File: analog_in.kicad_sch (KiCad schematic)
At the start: 0 parts

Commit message: Routed analog input and generator, added ethernet
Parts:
- added C2: 0.1, symbol Device:C
- added D5: TVS, Package_TO_SOT_SMD:SOT-23, symbol Diode:SM712_SOT23
- added R13, R14: 100, symbol Device:R
- added U2: INA600, Package_TO_SOT_SMD:SOT-23-6, symbol Amplifier_Current:INA181
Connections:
- new net: D5.1 (A1), R13.2, U2.3 (+)
- new net: D5.2 (A2), R14.2, U2.4 (-)
- new net +1V8: U2.5 (REF)
- new net +5V: C2.2, U2.6 (V+)
- new net AIN+: R13.1
- new net AIN-: R14.1
- new net AOUT: U2.1
- new net GND: C2.1, D5.3 (common), U2.2 (GND)

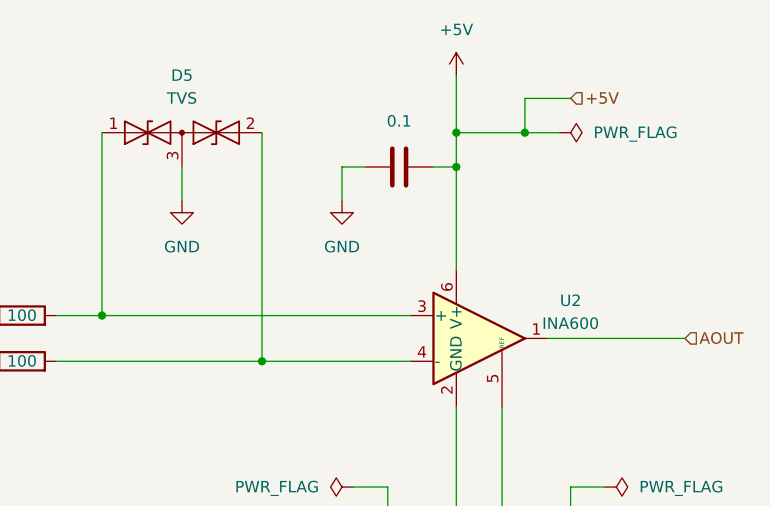
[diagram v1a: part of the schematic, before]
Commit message: Rearranged sheets and corrected some namings
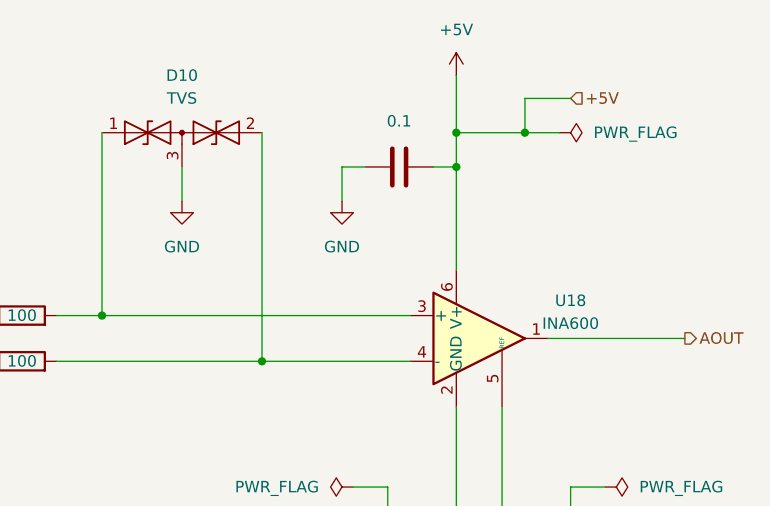
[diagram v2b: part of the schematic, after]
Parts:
- renumbered C2 to C40, D5 to D10, R13 to R43, R14 to R44, U2 to U18

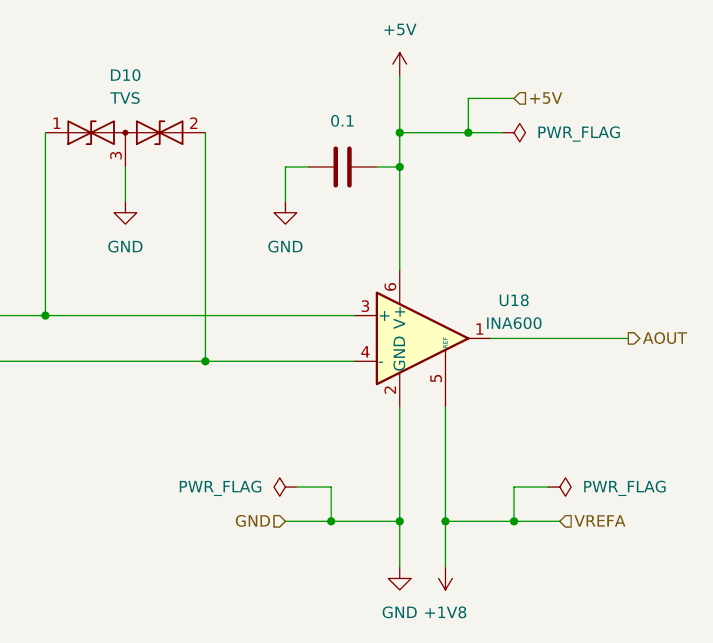
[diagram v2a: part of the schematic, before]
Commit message: Finished power setup and cleared some mistakes
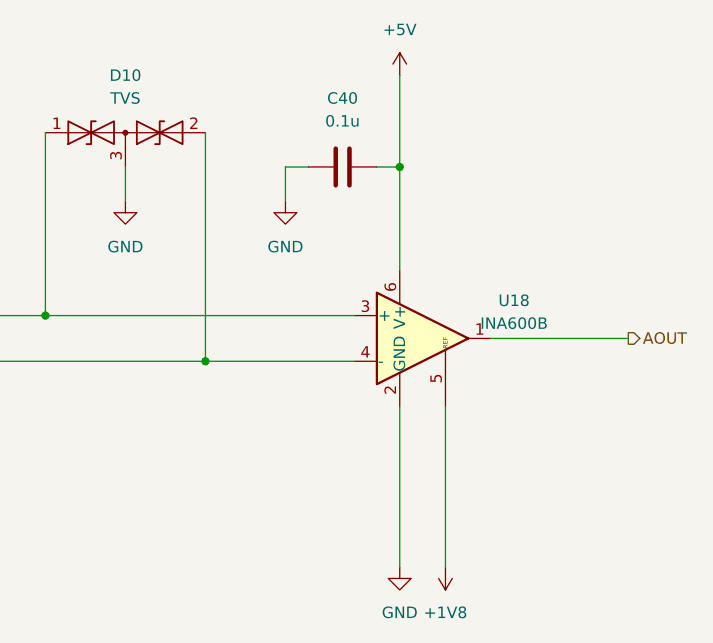
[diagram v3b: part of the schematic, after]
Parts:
- C40: value 0.1 -> 0.1u
- U18: value INA600 -> INA600B
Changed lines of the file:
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@@
 (kicad_sch (version 20230121) (generator eeschema)
   (paper "A4")
-  (junction (at 165.1 115.57) (diameter 0) (color 0 0 0 0)
-  )
-  (junction (at 165.1 72.39) (diameter 0) (color 0 0 0 0)
-  )
-  (junction (at 170.18 115.57) (diameter 0) (color 0 0 0 0)
-  )
-  (junction (at 172.72 72.39) (diameter 0) (color 0 0 0 0)
-  )
-  (junction (at 177.8 115.57) (diameter 0) (color 0 0 0 0)
-  )
-  (junction (at 157.48 115.57) (diameter 0) (color 0 0 0 0)
-  )
   (junction (at 165.1 76.2) (diameter 0) (color 0 0 0 0)
   )
@@
   (junction (at 143.51 97.79) (diameter 0) (color 0 0 0 0)
   )
-  (wire (pts (xy 170.18 115.57) (xy 177.8 115.57))
-    (stroke (width 0) (type default))
-  )
-  (wire (pts (xy 177.8 115.57) (xy 182.88 115.57))
-    (stroke (width 0) (type default))
-  )
-  (wire (pts (xy 181.61 111.76) (xy 177.8 111.76))
-    (stroke (width 0) (type default))
-  )
-  (wire (pts (xy 172.72 72.39) (xy 176.53 72.39))
-    (stroke (width 0) (type default))
-  )
   (wire (pts (xy 102.87 97.79) (xy 113.03 97.79))
     (stroke (width 0) (type default))
@@
     (stroke (width 0) (type default))
   )
-  (wire (pts (xy 157.48 111.76) (xy 157.48 115.57))
-    (stroke (width 0) (type default))
-  )
   (wire (pts (xy 143.51 97.79) (xy 160.02 97.79))
     (stroke (width 0) (type default))
   )
-  (wire (pts (xy 165.1 66.04) (xy 165.1 72.39))
-    (stroke (width 0) (type default))
-  )
-  (wire (pts (xy 152.4 115.57) (xy 157.48 115.57))
+  (wire (pts (xy 165.1 66.04) (xy 165.1 76.2))
     (stroke (width 0) (type default))
   )
@@
     (stroke (width 0) (type default))
   )
-  (wire (pts (xy 170.18 102.87) (xy 170.18 115.57))
+  (wire (pts (xy 170.18 102.87) (xy 170.18 120.65))
     (stroke (width 0) (type default))
   )
@@
     (stroke (width 0) (type default))
   )
-  (wire (pts (xy 165.1 102.87) (xy 165.1 115.57))
+  (wire (pts (xy 165.1 102.87) (xy 165.1 120.65))
     (stroke (width 0) (type default))
   )
@@
     (stroke (width 0) (type default))
   )
-  (wire (pts (xy 170.18 115.57) (xy 170.18 120.65))
-    (stroke (width 0) (type default))
-  )
-  (wire (pts (xy 165.1 72.39) (xy 165.1 76.2))
-    (stroke (width 0) (type default))
-  )
   (wire (pts (xy 102.87 92.71) (xy 113.03 92.71))
     (stroke (width 0) (type default))
   )
-  (wire (pts (xy 153.67 111.76) (xy 157.48 111.76))
-    (stroke (width 0) (type default))
-  )
-  (wire (pts (xy 177.8 111.76) (xy 177.8 115.57))
-    (stroke (width 0) (type default))
-  )
-  (wire (pts (xy 172.72 68.58) (xy 172.72 72.39))
-    (stroke (width 0) (type default))
-  )
   (wire (pts (xy 152.4 76.2) (xy 152.4 80.01))
     (stroke (width 0) (type default))
   )
-  (wire (pts (xy 177.8 68.58) (xy 172.72 68.58))
-    (stroke (width 0) (type default))
-  )
   (wire (pts (xy 125.73 72.39) (xy 125.73 92.71))
     (stroke (width 0) (type default))
   )
-  (wire (pts (xy 157.48 115.57) (xy 165.1 115.57))
-    (stroke (width 0) (type default))
-  )
   (wire (pts (xy 120.65 97.79) (xy 143.51 97.79))
     (stroke (width 0) (type default))
   )
-  (wire (pts (xy 165.1 115.57) (xy 165.1 120.65))
-    (stroke (width 0) (type default))
-  )
   (wire (pts (xy 143.51 72.39) (xy 143.51 97.79))
     (stroke (width 0) (type default))
   )
   (wire (pts (xy 134.62 76.2) (xy 134.62 80.01))
-    (stroke (width 0) (type default))
-  )
-  (wire (pts (xy 165.1 72.39) (xy 172.72 72.39))
     (stroke (width 0) (type default))
   )
@@
     (effects (font (size 1.27 1.27)) (justify left))
   )
-  (hierarchical_label "+5V" (shape input) (at 177.8 68.58 0) (fields_autoplaced)
-    (effects (font (size 1.27 1.27)) (justify left))
-  )
-  (hierarchical_label "GND" (shape input) (at 152.4 115.57 180) (fields_autoplaced)
-    (effects (font (size 1.27 1.27)) (justify right))
-  )
   (hierarchical_label "AIN+" (shape input) (at 102.87 92.71 180) (fields_autoplaced)
     (effects (font (size 1.27 1.27)) (justify right))
-  )
-  (hierarchical_label "VREFA" (shape input) (at 182.88 115.57 0) (fields_autoplaced)
-    (effects (font (size 1.27 1.27)) (justify left))
   )
   (hierarchical_label "AIN-" (shape input) (at 102.87 97.79 180) (fields_autoplaced)
@@
     (in_bom yes) (on_board yes) (dnp no) (fields_autoplaced)
     (property "Reference" "C40" (at 158.75 68.58 90)
-      (effects (font (size 1.27 1.27)) hide)
-    )
-    (property "Value" "0.1" (at 158.75 71.12 90)
+      (effects (font (size 1.27 1.27)))
+    )
+    (property "Value" "0.1u" (at 158.75 71.12 90)
       (effects (font (size 1.27 1.27)))
     )
@@
     )
   )
-  (symbol (lib_id "power:PWR_FLAG") (at 181.61 111.76 270) (unit 1)
-    (in_bom yes) (on_board yes) (dnp no) (fields_autoplaced)
-    (property "Reference" "#FLG042" (at 183.515 111.76 0)
-      (effects (font (size 1.27 1.27)) hide)
-    )
-    (property "Value" "PWR_FLAG" (at 185.42 111.76 90)
-      (effects (font (size 1.27 1.27)) (justify left))
-    )
-    (property "Footprint" "" (at 181.61 111.76 0)
-      (effects (font (size 1.27 1.27)) hide)
-    )
-    (property "Datasheet" "~" (at 181.61 111.76 0)
-      (effects (font (size 1.27 1.27)) hide)
-    )
-    (pin "1")
-    (instances
-      (project "cad-enc-dec"
-        (path "/894df1c3-1a5d-48b0-9966-84d5c2c2c705/3147f239-9a8b-459b-8889-8b3ae22f6154"
-          (reference "#FLG042") (unit 1)
-        )
-        (path "/894df1c3-1a5d-48b0-9966-84d5c2c2c705/48b865f7-3ad4-4ab2-8a39-622512f3cca3"
-          (reference "#FLG05") (unit 1)
-        )
-        (path "/894df1c3-1a5d-48b0-9966-84d5c2c2c705/6aec754e-1a09-4013-9dcc-eaf34b4a6299"
-          (reference "#FLG028") (unit 1)
-        )
-        (path "/894df1c3-1a5d-48b0-9966-84d5c2c2c705/03acb586-98c9-4180-936a-eaf01854a57a"
-          (reference "#FLG035") (unit 1)
-        )
-        (path "/894df1c3-1a5d-48b0-9966-84d5c2c2c705/0562ea40-d947-4895-9f9c-71efdb5c7549"
-          (reference "#FLG021") (unit 1)
-        )
-        (path "/894df1c3-1a5d-48b0-9966-84d5c2c2c705/04ed763c-fa4a-4a00-b73b-43854aeae6ba"
-          (reference "#FLG018") (unit 1)
-        )
-      )
-    )
-  )
-  (symbol (lib_id "power:PWR_FLAG") (at 153.67 111.76 90) (unit 1)
-    (in_bom yes) (on_board yes) (dnp no) (fields_autoplaced)
-    (property "Reference" "#FLG041" (at 151.765 111.76 0)
-      (effects (font (size 1.27 1.27)) hide)
-    )
-    (property "Value" "PWR_FLAG" (at 149.86 111.76 90)
-      (effects (font (size 1.27 1.27)) (justify left))
-    )
-    (property "Footprint" "" (at 153.67 111.76 0)
-      (effects (font (size 1.27 1.27)) hide)
-    )
-    (property "Datasheet" "~" (at 153.67 111.76 0)
-      (effects (font (size 1.27 1.27)) hide)
-    )
-    (pin "1")
-    (instances
-      (project "cad-enc-dec"
-        (path "/894df1c3-1a5d-48b0-9966-84d5c2c2c705/3147f239-9a8b-459b-8889-8b3ae22f6154"
-          (reference "#FLG041") (unit 1)
-        )
-        (path "/894df1c3-1a5d-48b0-9966-84d5c2c2c705/48b865f7-3ad4-4ab2-8a39-622512f3cca3"
-          (reference "#FLG04") (unit 1)
-        )
-        (path "/894df1c3-1a5d-48b0-9966-84d5c2c2c705/6aec754e-1a09-4013-9dcc-eaf34b4a6299"
-          (reference "#FLG025") (unit 1)
-        )
-        (path "/894df1c3-1a5d-48b0-9966-84d5c2c2c705/03acb586-98c9-4180-936a-eaf01854a57a"
-          (reference "#FLG034") (unit 1)
-        )
-        (path "/894df1c3-1a5d-48b0-9966-84d5c2c2c705/0562ea40-d947-4895-9f9c-71efdb5c7549"
-          (reference "#FLG020") (unit 1)
-        )
-        (path "/894df1c3-1a5d-48b0-9966-84d5c2c2c705/04ed763c-fa4a-4a00-b73b-43854aeae6ba"
-          (reference "#FLG017") (unit 1)
-        )
-      )
-    )
-  )
   (symbol (lib_id "Amplifier_Current:INA181") (at 167.64 95.25 0) (unit 1)
     (in_bom yes) (on_board yes) (dnp no) (fields_autoplaced)
@@
       (effects (font (size 1.27 1.27)))
     )
-    (property "Value" "INA600" (at 177.8 93.5991 0)
+    (property "Value" "INA600B" (at 177.8 93.5991 0)
       (effects (font (size 1.27 1.27)))
     )
@@
         )
       )
-    )
-  )
-  (symbol (lib_id "power:PWR_FLAG") (at 176.53 72.39 270) (unit 1)
-    (in_bom yes) (on_board yes) (dnp no) (fields_autoplaced)
-    (property "Reference" "#FLG040" (at 178.435 72.39 0)
-      (effects (font (size 1.27 1.27)) hide)
-    )
-    (property "Value" "PWR_FLAG" (at 180.34 72.39 90)
-      (effects (font (size 1.27 1.27)) (justify left))
-    )
-    (property "Footprint" "" (at 176.53 72.39 0)
-      (effects (font (size 1.27 1.27)) hide)
-    )
-    (property "Datasheet" "~" (at 176.53 72.39 0)
-      (effects (font (size 1.27 1.27)) hide)
-    )
-    (pin "1")
-    (instances
-      (project "cad-enc-dec"
-        (path "/894df1c3-1a5d-48b0-9966-84d5c2c2c705/3147f239-9a8b-459b-8889-8b3ae22f6154"
-          (reference "#FLG040") (unit 1)
-        )
-        (path "/894df1c3-1a5d-48b0-9966-84d5c2c2c705/48b865f7-3ad4-4ab2-8a39-622512f3cca3"
-          (reference "#FLG03") (unit 1)
-        )
-        (path "/894df1c3-1a5d-48b0-9966-84d5c2c2c705/6aec754e-1a09-4013-9dcc-eaf34b4a6299"
-          (reference "#FLG024") (unit 1)
-        )
-        (path "/894df1c3-1a5d-48b0-9966-84d5c2c2c705/03acb586-98c9-4180-936a-eaf01854a57a"
-          (reference "#FLG033") (unit 1)
-        )
-        (path "/894df1c3-1a5d-48b0-9966-84d5c2c2c705/0562ea40-d947-4895-9f9c-71efdb5c7549"
-          (reference "#FLG019") (unit 1)
-        )
-        (path "/894df1c3-1a5d-48b0-9966-84d5c2c2c705/04ed763c-fa4a-4a00-b73b-43854aeae6ba"
-          (reference "#FLG016") (unit 1)
-        )
-      )

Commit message: Polished IO schematics
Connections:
- net +1V8 renamed VREFAIN
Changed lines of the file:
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@@
-    (stroke (width 0) (type default))
-  )
-  (wire (pts (xy 170.18 102.87) (xy 170.18 120.65))
     (stroke (width 0) (type default))
   )
@@
     (stroke (width 0) (type default))
   )
+  (wire (pts (xy 170.18 102.87) (xy 170.18 105.41))
+    (stroke (width 0) (type default))
+  )
   (wire (pts (xy 102.87 92.71) (xy 113.03 92.71))
+    (stroke (width 0) (type default))
+  )
+  (wire (pts (xy 139.7 105.41) (xy 170.18 105.41))
     (stroke (width 0) (type default))
   )
@@
   (wire (pts (xy 134.62 76.2) (xy 134.62 80.01))
     (stroke (width 0) (type default))
+  )
+  (hierarchical_label "VREFAIN" (shape input) (at 139.7 105.41 180) (fields_autoplaced)
+    (effects (font (size 1.27 1.27)) (justify right))
   )
   (hierarchical_label "AOUT" (shape output) (at 190.5 95.25 0) (fields_autoplaced)
@@
         )
       )
-    )
-  )
-  (symbol (lib_id "power:+1V8") (at 170.18 120.65 180) (unit 1)
-    (in_bom yes) (on_board yes) (dnp no) (fields_autoplaced)
-    (property "Reference" "#PWR073" (at 170.18 116.84 0)
-      (effects (font (size 1.27 1.27)) hide)
-    )
-    (property "Value" "+1V8" (at 170.18 125.73 0)
-      (effects (font (size 1.27 1.27)))
-    )
-    (property "Footprint" "" (at 170.18 120.65 0)
-      (effects (font (size 1.27 1.27)) hide)
-    )
-    (property "Datasheet" "" (at 170.18 120.65 0)
-      (effects (font (size 1.27 1.27)) hide)
-    )
-    (pin "1")
-    (instances
-      (project "cad-enc-dec"
-        (path "/894df1c3-1a5d-48b0-9966-84d5c2c2c705/3147f239-9a8b-459b-8889-8b3ae22f6154"
-          (reference "#PWR073") (unit 1)
-        )
-        (path "/894df1c3-1a5d-48b0-9966-84d5c2c2c705/48b865f7-3ad4-4ab2-8a39-622512f3cca3"
-          (reference "#PWR012") (unit 1)
-        )
-        (path "/894df1c3-1a5d-48b0-9966-84d5c2c2c705/6aec754e-1a09-4013-9dcc-eaf34b4a6299"
-          (reference "#PWR051") (unit 1)
-        )
-        (path "/894df1c3-1a5d-48b0-9966-84d5c2c2c705/03acb586-98c9-4180-936a-eaf01854a57a"
-          (reference "#PWR062") (unit 1)
-        )
-        (path "/894df1c3-1a5d-48b0-9966-84d5c2c2c705/0562ea40-d947-4895-9f9c-71efdb5c7549"
-          (reference "#PWR043") (unit 1)
-        )
-        (path "/894df1c3-1a5d-48b0-9966-84d5c2c2c705/04ed763c-fa4a-4a00-b73b-43854aeae6ba"
-          (reference "#PWR038") (unit 1)
-        )
-      )
